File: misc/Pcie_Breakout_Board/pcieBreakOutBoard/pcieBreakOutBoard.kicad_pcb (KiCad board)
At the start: 2 copper layers, 49.5 x 36.8 mm, 4 parts, among them J1 2041119-1 (Mini Pcie Express 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, J2 Conn_01x14, J3 Conn_01x14, J4 Conn_02x12_Odd_Even

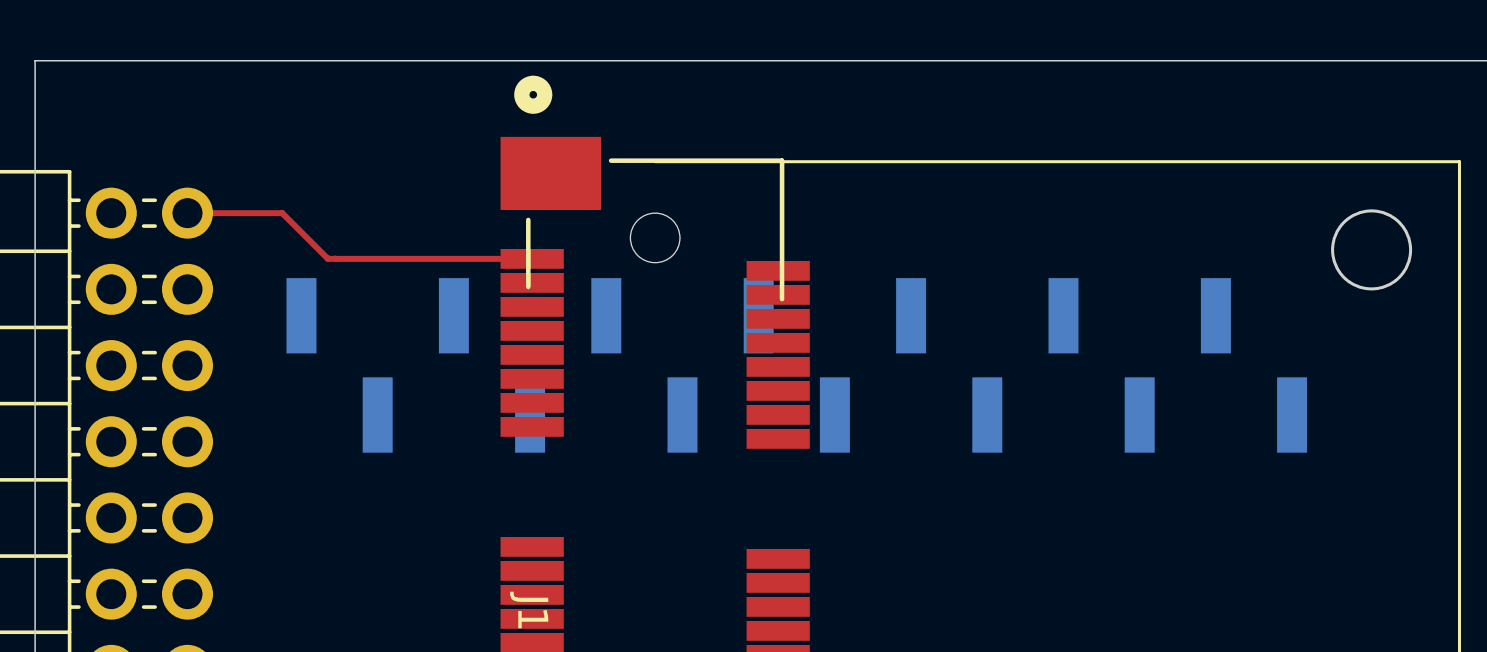
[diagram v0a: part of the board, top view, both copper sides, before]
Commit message: PCI Express
Create breakout board for the PCI express mini card half
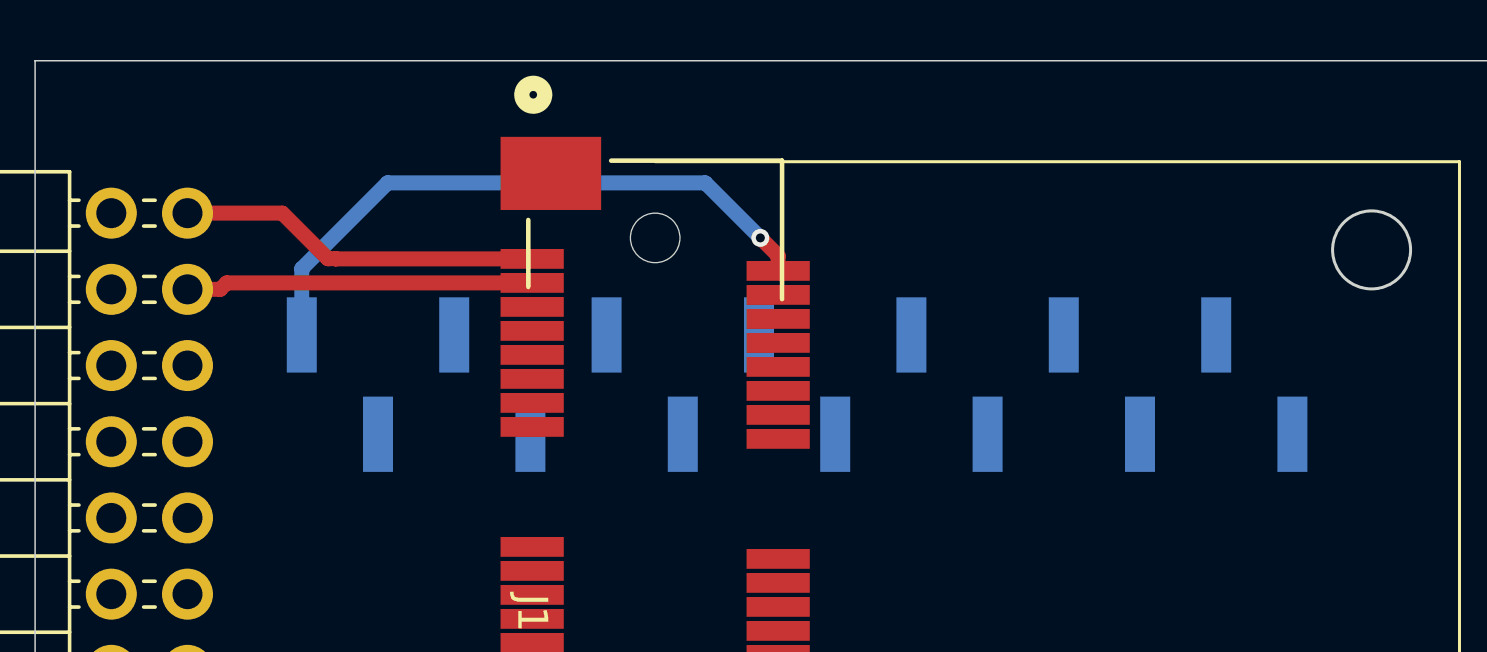
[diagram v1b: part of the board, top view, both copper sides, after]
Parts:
- moved J2 0.64 mm to (144.8, 87.0), turned to 90 degrees
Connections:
- J1 pad 10: unconnected-(J1-Pad10) -> /Port10
- J1 pad 11: unconnected-(J1-Pad11) -> /Port11
- J1 pad 12: unconnected-(J1-Pad12) -> /Port12
- J1 pad 13: unconnected-(J1-Pad13) -> /Port13
- J1 pad 14: unconnected-(J1-Pad14) -> /Port14
- J1 pad 15: unconnected-(J1-Pad15) -> /Port15
- J1 pad 16: unconnected-(J1-Pad16) -> /Port16
- J1 pad 17: unconnected-(J1-Pad17) -> /Port17
- J1 pad 18: unconnected-(J1-Pad18) -> /Port18
- J1 pad 19: unconnected-(J1-Pad19) -> /Port19
- J1 pad 2: unconnected-(J1-Pad2) -> /Port2
- J1 pad 20: unconnected-(J1-Pad20) -> /Port20
- J1 pad 21: unconnected-(J1-Pad21) -> /Port21
- J1 pad 22: unconnected-(J1-Pad22) -> /Port22
- J1 pad 23: unconnected-(J1-Pad23) -> /Port23
- J1 pad 24: unconnected-(J1-Pad24) -> /Port24
- J1 pad 25: unconnected-(J1-Pad25) -> /Port25
- J1 pad 26: unconnected-(J1-Pad26) -> /Port26
- J1 pad 27: unconnected-(J1-Pad27) -> /Port27
- J1 pad 28: unconnected-(J1-Pad28) -> /Port28
- J1 pad 29: unconnected-(J1-Pad29) -> /Port29
- J1 pad 3: /Port2 -> /Port3
- J1 pad 30: unconnected-(J1-Pad30) -> /Port30
- J1 pad 31: unconnected-(J1-Pad31) -> /Port31
- J1 pad 32: unconnected-(J1-Pad32) -> /Port32
- J1 pad 33: unconnected-(J1-Pad33) -> /Port33
- J1 pad 34: unconnected-(J1-Pad34) -> /Port34
- J1 pad 35: unconnected-(J1-Pad35) -> /Port35
- J1 pad 36: unconnected-(J1-Pad36) -> /Port36
- J1 pad 37: unconnected-(J1-Pad37) -> /Port37
- J1 pad 38: unconnected-(J1-Pad38) -> /Port38
- J1 pad 39: unconnected-(J1-Pad39) -> /Port39
- J1 pad 4: unconnected-(J1-Pad4) -> /Port4
- J1 pad 40: unconnected-(J1-Pad40) -> /Port40
- J1 pad 41: unconnected-(J1-Pad41) -> /Port41
- J1 pad 42: unconnected-(J1-Pad42) -> /Port42
- J1 pad 43: unconnected-(J1-Pad43) -> /Port43
- J1 pad 44: unconnected-(J1-Pad44) -> /Port44
- J1 pad 45: unconnected-(J1-Pad45) -> /Port45
- J1 pad 46: unconnected-(J1-Pad46) -> /Port46
- J1 pad 47: unconnected-(J1-Pad47) -> /Port47
- J1 pad 48: unconnected-(J1-Pad48) -> /Port48
- J1 pad 49: unconnected-(J1-Pad49) -> /Port49
- J1 pad 5: unconnected-(J1-Pad5) -> /Port5
- J1 pad 50: unconnected-(J1-Pad50) -> /Port50
- J1 pad 51: unconnected-(J1-Pad51) -> /Port51
- J1 pad 52: unconnected-(J1-Pad52) -> /Port52
- J1 pad 6: unconnected-(J1-Pad6) -> /Port6
- J1 pad 7: unconnected-(J1-Pad7) -> /Port7
- J1 pad 8: unconnected-(J1-Pad8) -> /Port8
- J1 pad 9: unconnected-(J1-Pad9) -> /Port9
- J2 pad 14: unconnected-(J2-Pin_14-Pad14) -> /Port2
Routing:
- net /Port2: track 0.00 -> 20.8 mm, vias 0 -> 1
- net /Port3: track 0.00 -> 11.6 mm

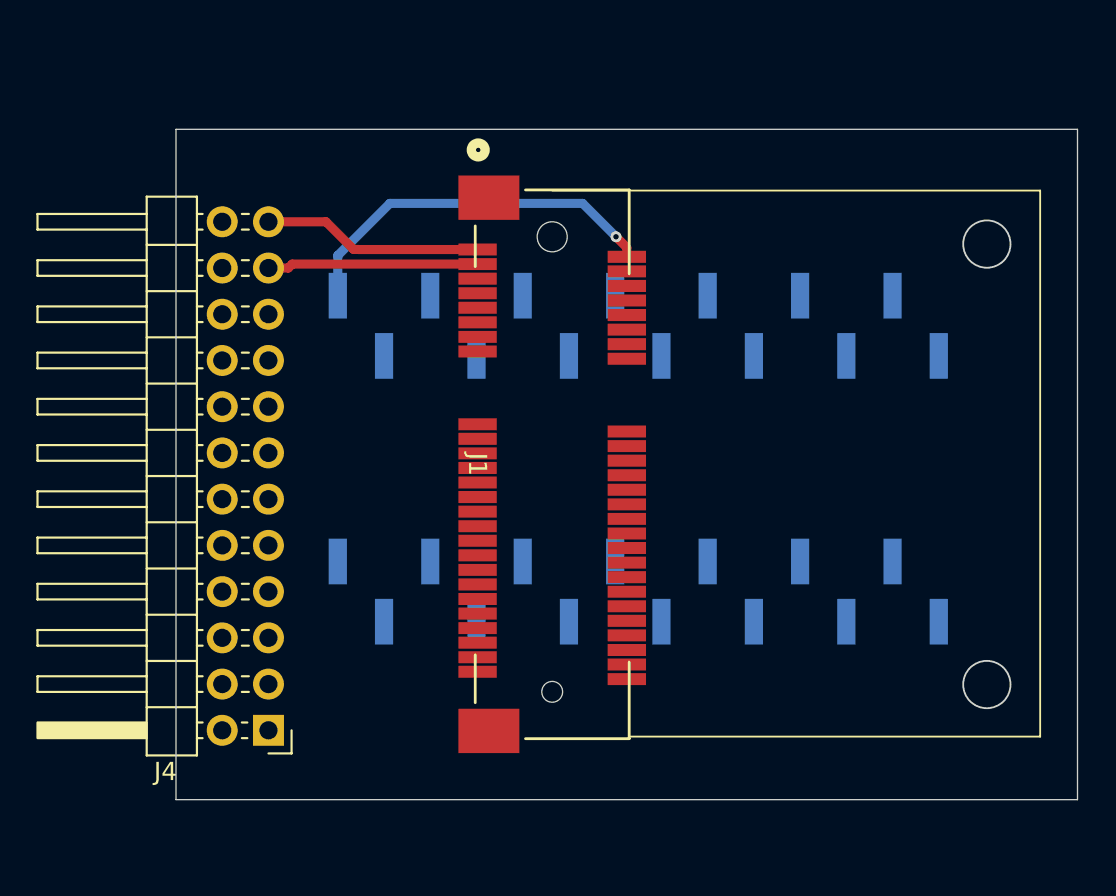
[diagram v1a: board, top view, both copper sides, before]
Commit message: pci express Breakoutt Board
Finished routing
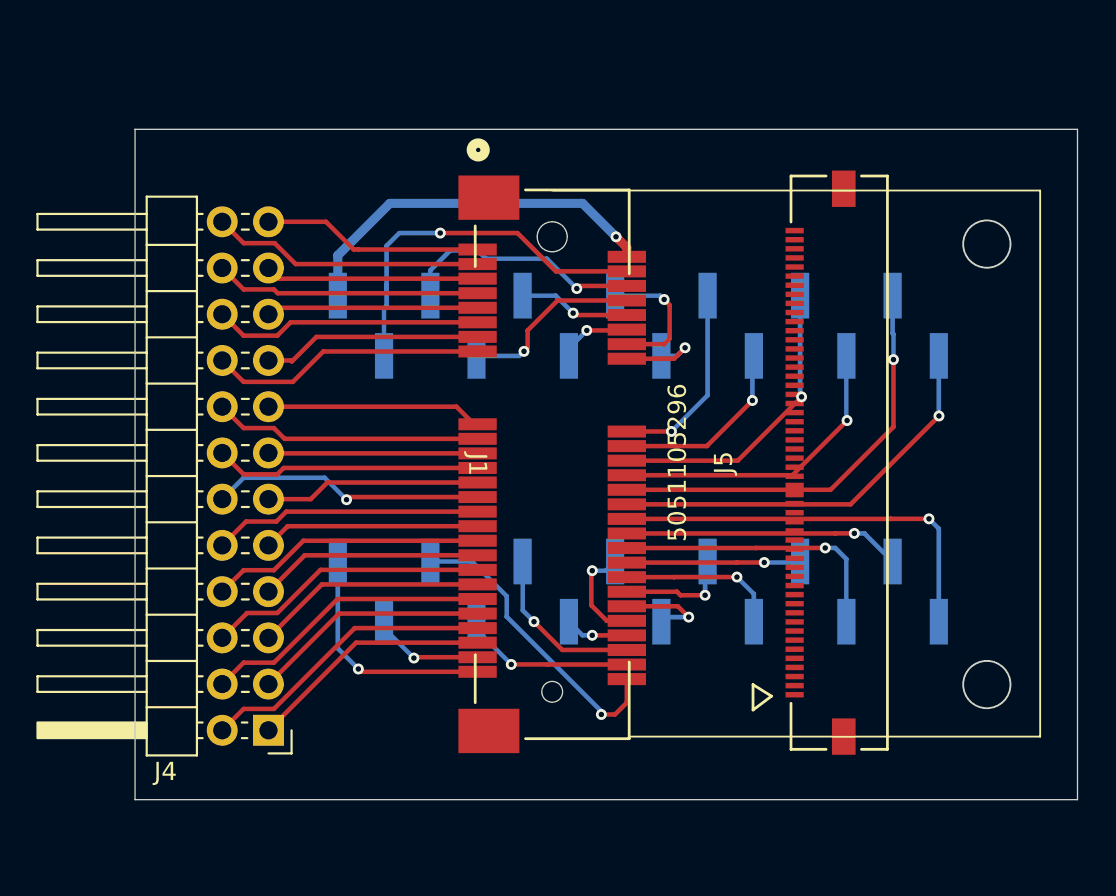
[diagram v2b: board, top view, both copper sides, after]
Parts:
- added J5: 5051105296, User_Footprint:CON_5051105296_MOL, F.Cu at (155.8, 94.5)
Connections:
- J2 pad 1: unconnected-(J2-Pin_1-Pad1) -> /Port28
- J2 pad 10: unconnected-(J2-Pin_10-Pad10) -> /Port10
- J2 pad 11: unconnected-(J2-Pin_11-Pad11) -> /Port8
- J2 pad 12: unconnected-(J2-Pin_12-Pad12) -> /Port6
- J2 pad 13: unconnected-(J2-Pin_13-Pad13) -> /Port4
- J2 pad 2: unconnected-(J2-Pin_2-Pad2) -> /Port26
- J2 pad 3: unconnected-(J2-Pin_3-Pad3) -> /Port24
- J2 pad 4: unconnected-(J2-Pin_4-Pad4) -> /Port22
- J2 pad 5: unconnected-(J2-Pin_5-Pad5) -> /Port20
- J2 pad 6: unconnected-(J2-Pin_6-Pad6) -> /Port18
- J2 pad 7: unconnected-(J2-Pin_7-Pad7) -> /Port16
- J2 pad 8: unconnected-(J2-Pin_8-Pad8) -> /Port14
- J2 pad 9: unconnected-(J2-Pin_9-Pad9) -> /Port12
- J3 pad 1: unconnected-(J3-Pin_1-Pad1) -> /Port51
- J3 pad 10: unconnected-(J3-Pin_10-Pad10) -> /Port38
- J3 pad 11: unconnected-(J3-Pin_11-Pad11) -> /Port36
- J3 pad 12: unconnected-(J3-Pin_12-Pad12) -> /Port34
- J3 pad 13: unconnected-(J3-Pin_13-Pad13) -> /Port32
- J3 pad 14: unconnected-(J3-Pin_14-Pad14) -> /Port30
- J3 pad 2: unconnected-(J3-Pin_2-Pad2) -> /Port49
- J3 pad 3: unconnected-(J3-Pin_3-Pad3) -> /Port52
- J3 pad 4: unconnected-(J3-Pin_4-Pad4) -> /Port50
- J3 pad 5: unconnected-(J3-Pin_5-Pad5) -> /Port48
- J3 pad 6: unconnected-(J3-Pin_6-Pad6) -> /Port46
- J3 pad 7: unconnected-(J3-Pin_7-Pad7) -> /Port44
- J3 pad 8: unconnected-(J3-Pin_8-Pad8) -> /Port42
- J3 pad 9: unconnected-(J3-Pin_9-Pad9) -> /Port40
- J4 pad 1: unconnected-(J4-Pin_1-Pad1) -> /Port47
- J4 pad 10: unconnected-(J4-Pin_10-Pad10) -> /Port29
- J4 pad 11: unconnected-(J4-Pin_11-Pad11) -> /Port25
- J4 pad 12: unconnected-(J4-Pin_12-Pad12) -> /Port27
- J4 pad 13: unconnected-(J4-Pin_13-Pad13) -> /Port21
- J4 pad 14: unconnected-(J4-Pin_14-Pad14) -> /Port23
- J4 pad 15: unconnected-(J4-Pin_15-Pad15) -> /Port17
- J4 pad 16: unconnected-(J4-Pin_16-Pad16) -> /Port19
- J4 pad 17: unconnected-(J4-Pin_17-Pad17) -> /Port13
- J4 pad 18: unconnected-(J4-Pin_18-Pad18) -> /Port15
- J4 pad 19: unconnected-(J4-Pin_19-Pad19) -> /Port9
- J4 pad 2: unconnected-(J4-Pin_2-Pad2) -> /Port45
- J4 pad 20: unconnected-(J4-Pin_20-Pad20) -> /Port11
- J4 pad 21: unconnected-(J4-Pin_21-Pad21) -> /Port5
- J4 pad 22: unconnected-(J4-Pin_22-Pad22) -> /Port7
- J4 pad 24: unconnected-(J4-Pin_24-Pad24) -> /Port3
- J4 pad 3: unconnected-(J4-Pin_3-Pad3) -> /Port43
- J4 pad 4: unconnected-(J4-Pin_4-Pad4) -> /Port41
- J4 pad 5: unconnected-(J4-Pin_5-Pad5) -> /Port39
- J4 pad 6: unconnected-(J4-Pin_6-Pad6) -> /Port37
- J4 pad 7: unconnected-(J4-Pin_7-Pad7) -> /Port35
- J4 pad 8: unconnected-(J4-Pin_8-Pad8) -> /Port33
- J4 pad 9: unconnected-(J4-Pin_9-Pad9) -> /Port31
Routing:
- net /Port26: track 0.00 -> 23.3 mm, vias 0 -> 1
- net /Port30: track 0.00 -> 22.5 mm, vias 0 -> 1
- net /Port28: track 0.00 -> 22.5 mm, vias 0 -> 1
- net /Port4: track 0.00 -> 20.7 mm, vias 0 -> 1
- net /Port24: track 0.00 -> 16.9 mm, vias 0 -> 1
- net /Port22: track 0.00 -> 16.6 mm, vias 0 -> 1
- net /Port52: track 0.00 -> 16.6 mm, vias 0 -> 1
- net /Port45: track 0.00 -> 16.4 mm
- net /Port41: track 0.00 -> 16.0 mm
- net /Port34: track 0.00 -> 15.8 mm, vias 0 -> 1
- net /Port37: track 0.00 -> 15.6 mm
- net /Port32: track 0.00 -> 15.2 mm, vias 0 -> 1
- net /Port15: track 0.00 -> 15.2 mm
- net /Port33: track 0.00 -> 15.2 mm
- net /Port27: track 0.00 -> 15.1 mm, vias 0 -> 1
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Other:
- board size 49.5 x 36.8 mm -> 51.8 x 36.8 mm

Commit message: dirctories
Add and remove directories
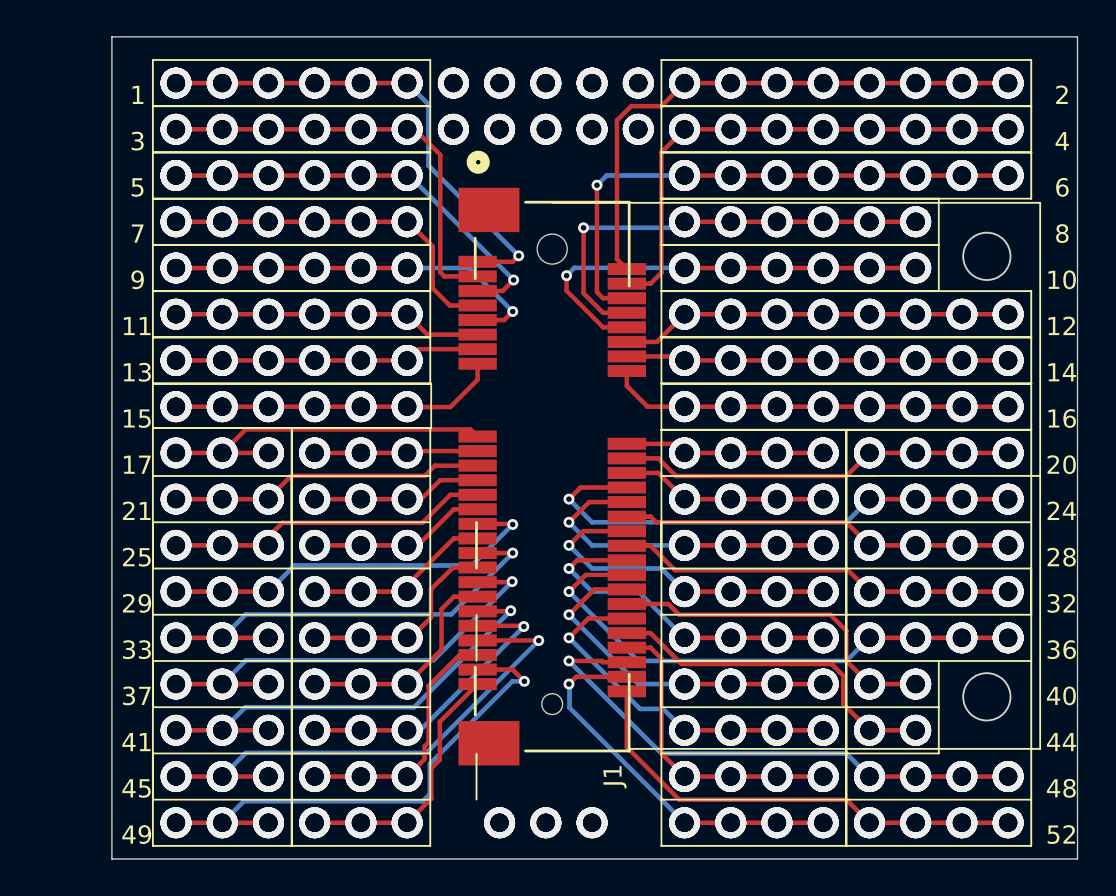
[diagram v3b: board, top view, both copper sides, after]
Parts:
- removed J2, J3: Conn_01x14, Connector_PinHeader_2.54mm:PinHeader_1x14_P2.54mm_Vertical_SMD_Pin1Left
- removed J4: Conn_02x12_Odd_Even, Connector_PinHeader_2.54mm:PinHeader_2x12_P2.54mm_Horizontal
- removed J5: 5051105296, User_Footprint:CON_5051105296_MOL
- moved J1 0.67 mm to (140.0, 95.3)
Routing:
- net /Port49: track 6.26 -> 28.7 mm, vias 1 -> 10
- net /Port48: track 9.33 -> 30.0 mm, vias 1 -> 13
- net /Port36: track 9.55 -> 29.8 mm, vias 1 -> 13
- net /Port10: track 6.16 -> 24.3 mm, vias 1 -> 19
- net /Port12: track 4.02 -> 21.6 mm, vias 1 -> 24
- net /Port16: track 4.94 -> 22.3 mm, vias 1 -> 24
- net /Port6: track 13.6 -> 30.5 mm, vias 1 -> 25
- net /Port1: track 12.1 -> 27.1 mm, vias 0 -> 19
- net /Port8: track 10.1 -> 24.8 mm, vias 1 -> 19
- net /Port42: track 5.25 -> 19.7 mm, vias 1 -> 13
- net /Port14: track 7.53 -> 21.0 mm, vias 1 -> 24
- net /Port44: track 5.69 -> 19.0 mm, vias 1 -> 6
- net /Port46: track 3.49 -> 16.8 mm, vias 1 -> 12
- net /Port45: track 16.4 -> 28.9 mm, vias 0 -> 9
- net /Port40: track 6.29 -> 18.7 mm, vias 1 -> 6
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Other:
- board size 51.8 x 36.8 mm -> 53 x 45.2 mm
- board text added: "1"
- board text added: "10"
- board text added: "11"
- board text added: "12"
- board text added: "13"
- board text added: "14"
- board text added: "15"
- board text added: "16"
- board text added: "17"
- board text added: "18"
- board text added: "19"
- board text added: "2"
- board text added: "20"
- board text added: "21"
- board text added: "22"
- board text added: "23"
- board text added: "24"
- board text added: "25"
- board text added: "26"
- board text added: "27"
- board text added: "28"
- board text added: "29"
- board text added: "3"
- board text added: "30"
- board text added: "31"
- board text added: "32"
- board text added: "33"
- board text added: "34"
- board text added: "35"
- board text added: "36"
- board text added: "37"
- board text added: "38"
- board text added: "39"
- board text added: "4"
- board text added: "40"
- board text added: "41"
- board text added: "42"
- board text added: "43"
- board text added: "44"
- board text added: "45"
- board text added: "46"
- board text added: "47"
- board text added: "48"
- board text added: "49"
- board text added: "5"
- board text added: "50"
- board text added: "51"
- board text added: "52"
- board text added: "6"
- board text added: "7"
- board text added: "8"
- board text added: "9"
